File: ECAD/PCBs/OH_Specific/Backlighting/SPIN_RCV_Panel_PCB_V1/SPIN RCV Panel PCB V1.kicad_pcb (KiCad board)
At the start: 2 copper layers, 45.7 x 168.3 mm, 66 parts, among them J1 Conn_01x04_Female, J2 Conn_01x04_Female

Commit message: Latest backlighting changes
Update to multiple PCBs, mainly changing from micro-fit to mini-fit connectors.
Also changing from individual power rails to filled copper planes where possible.
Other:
- board text added: "Version 2.0"
- board text removed: "Version 1.0"

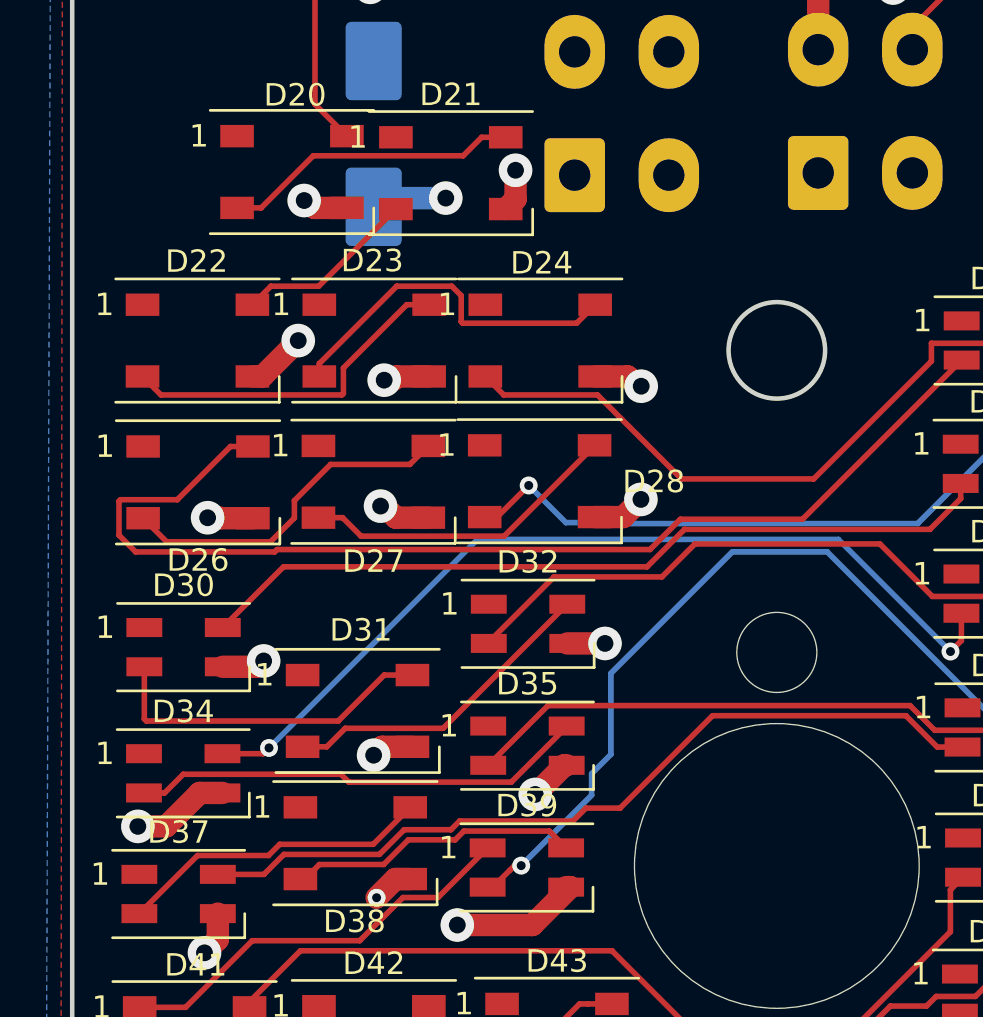
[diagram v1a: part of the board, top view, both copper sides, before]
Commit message: Backlighting PCB Updates
Added - Master mode button mounting holes to Master Arm panel
Added - ECM Jett button mounting holes to ECM JETT panel.
Added - Silkscreens to VID RCD PCB
Added - Ready LED to VID RCD PCB
Added - Manufacturing files for VID RCD PCB
Added - Manufacturing files for SPIN RCVY PCB
Added - Manufacturing files for MASTER ARM PCB
Added - Manufacturing files for ECM JETT PCB
Added - Manufacturing files for HUD PCB
Added - Manufacturing files for DEFOG LEVER PCB
Added - Manufacturing files for AV COOL PCB
Added - Manufacturing files for LDG WING FOLD PCB
Added - Extra backlighting string port to power distro PCB
Added - External power input connector to power distro PCB if ATX PSU cannot provide enough 5V current.
Added - Fan voltage selector on power distro PCB
Changed - Power distro PCB is now a solid copper fill on both sides to improve voltage drop under load.
Changed - VID RCD panel connectors to mini-fit
Changed - VID RCD panel LED pads from solid to thermal relief.
Changed - ECM JETT panel LED pads from solid to thermal relief.
Changed - MASTER ARM panel LED pads from solid to thermal relief.
Changed - SPIN RCVY panel LED pads from solid to thermal relief.
Changed - INTR LT panel LED pads from solid to thermal relief.
Changed - AV COOL panel LED pads from solid to thermal relief.
Changed - LDG WING FOLD panel LED pads from solid to thermal relief.
Changed - HUD panel LED pads from solid to thermal relief.
Changed - HUD panel connectors to mini-fit
Changed - JETT STATION SELECT PLACARD PCB connector to mini-fit
Fixed - Fan headers on power distro PCB mis-wired.
Removed - 1 row of LEDs on DEFOG PCB to improve reparability.
Removed - Version 1 folder from repo when it is replaced with a version 2 folder.
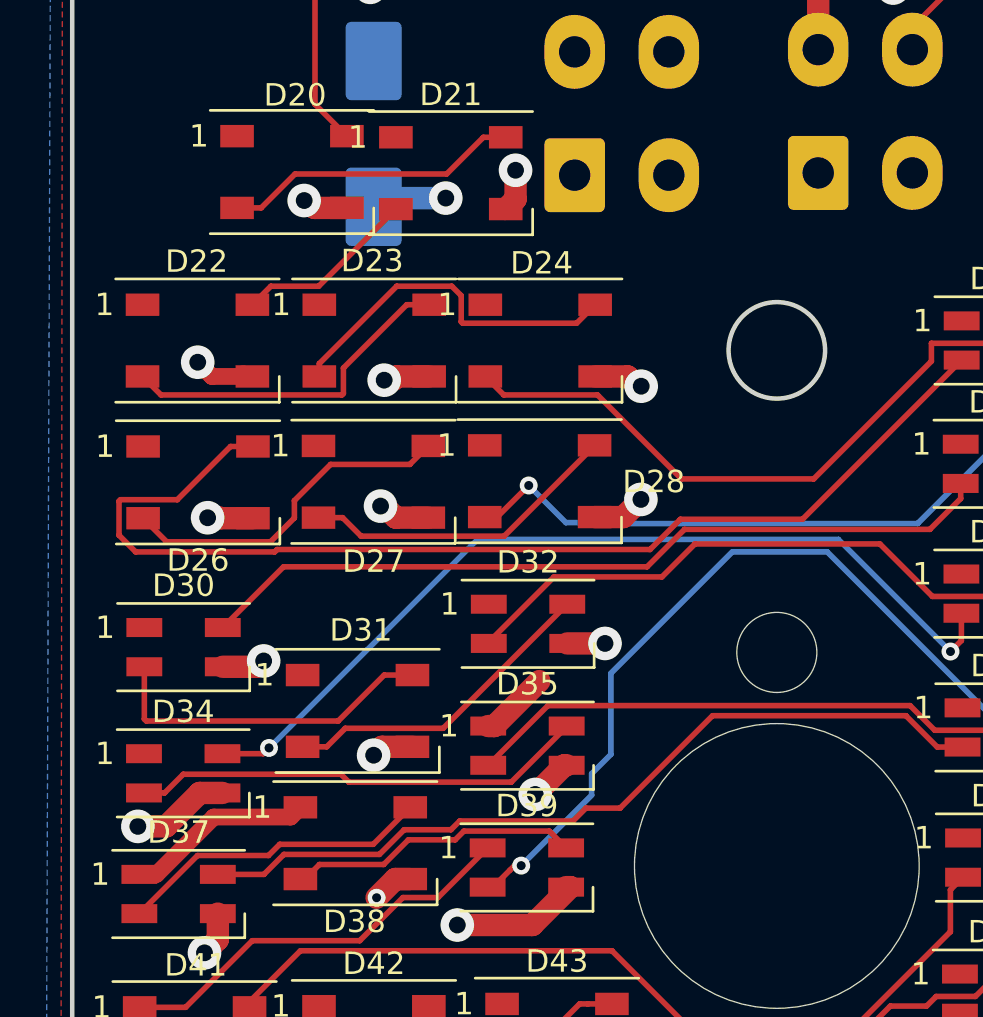
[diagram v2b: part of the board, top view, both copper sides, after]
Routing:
- net /LED+5V: track 54.2 -> 65.8 mm

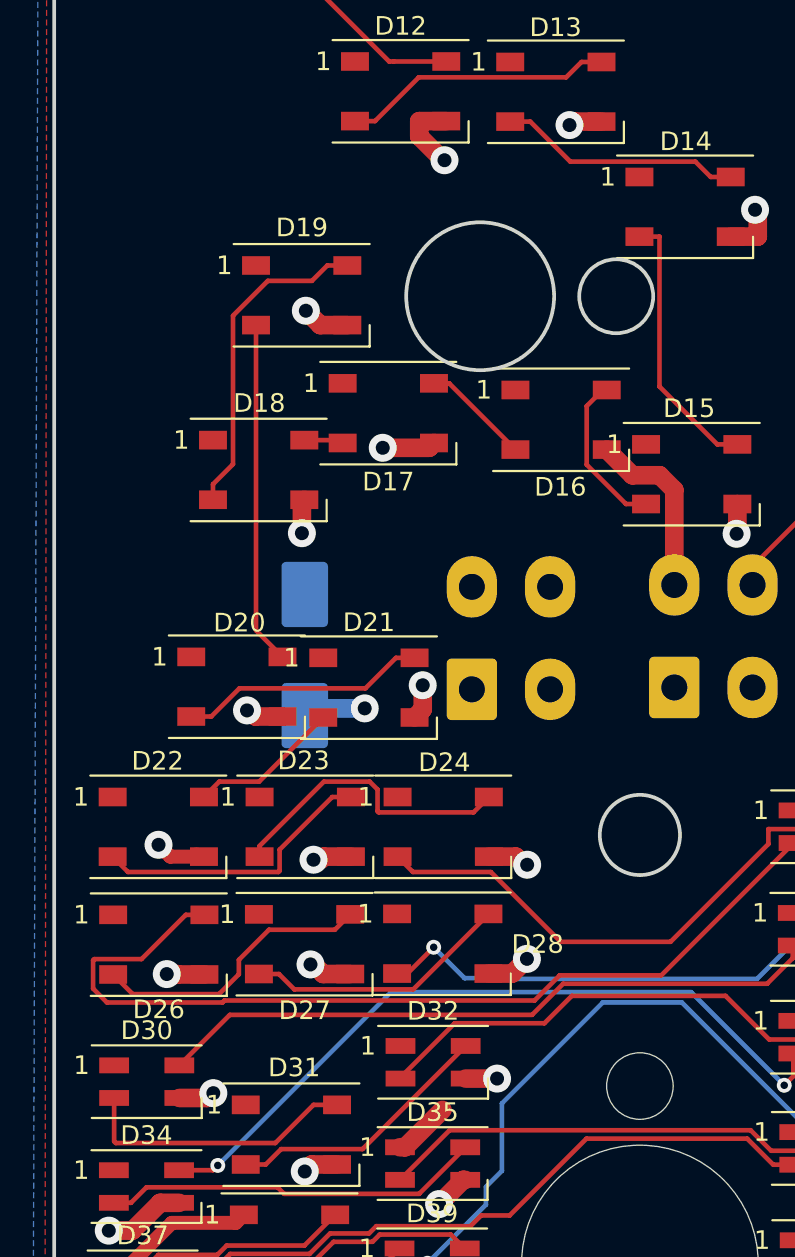
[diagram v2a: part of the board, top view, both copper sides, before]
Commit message: GEN TIE Panel overhaul and backlighting added.
Added - Gen Tie panel lightplate
Added - Gen Tie panel legend plate
Added - Gen Tie panel backlighting PCB
Added - Gen Tie panel backlighting PCB MCAD model to Gen Tie panel MCAD assembly.
Moved - ABSIS backlighting controller manufacturing files to a folder called manufacturing
Added - Fabrication notes to ABSIS backlighting controller PCB.
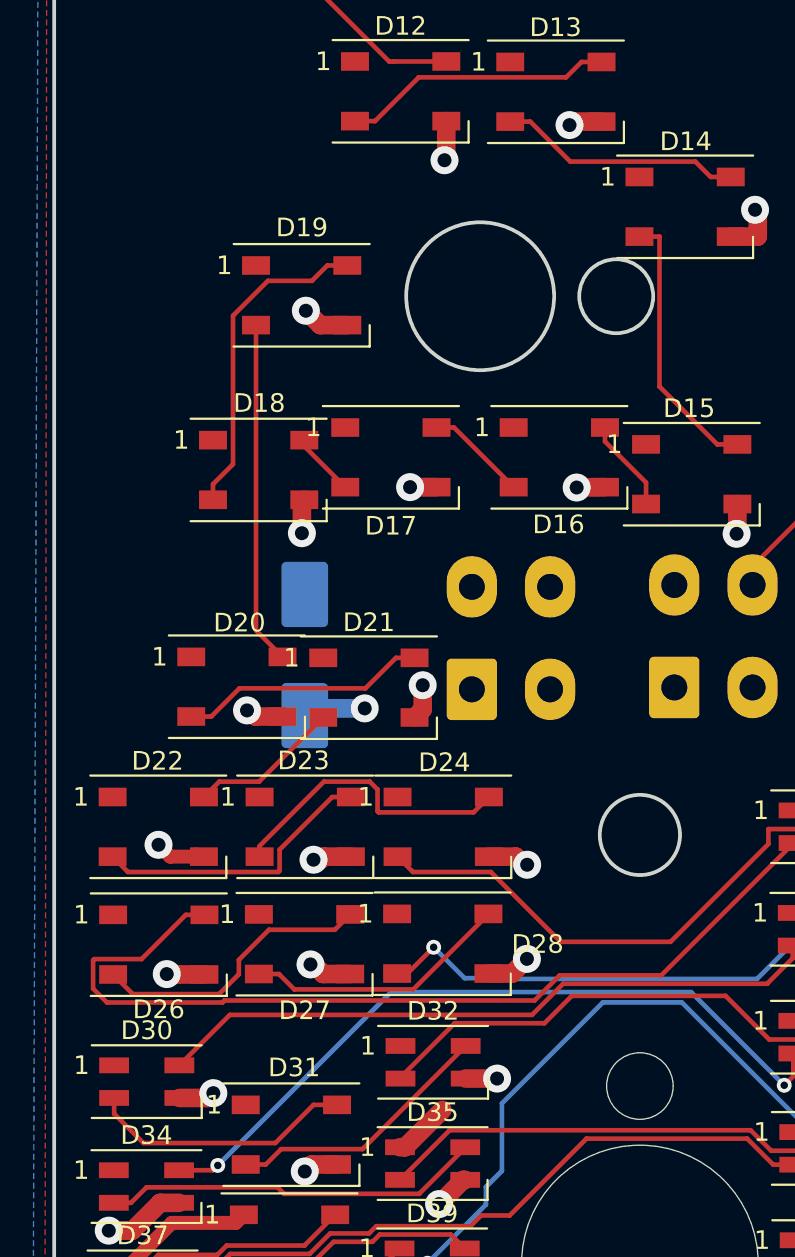
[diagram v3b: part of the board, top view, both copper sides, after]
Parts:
- moved D17 2.37 mm to (248.7, 90.0)
- moved D16 2.02 mm to (257.7, 90.0)
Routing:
- net /LEDGND: track 131.6 -> 120.0 mm, vias 52 -> 53
- net Net-(D15-Pad2): track 8.64 -> 5.02 mm
- net Net-(D17-Pad2): track 2.12 -> 3.43 mm
- net Net-(D30-Pad2): track 15.2 -> 14.3 mm
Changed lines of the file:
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@@
-(kicad_pcb (version 20171130) (host pcbnew "(5.1.6)-1")
+(kicad_pcb (version 20171130) (host pcbnew "(5.1.10)-1")
   (general
     (thickness 1.6)
-    (drawings 236)
-    (tracks 546)
+    (drawings 237)
+    (tracks 541)
     (zones 0)
     (modules 66)
@@
   )
   (module LED_SMD:LED_WS2812B_PLCC4_5.0x5.0mm_P3.2mm (layer F.Cu)
-    (at 248.553 87.579)
+    (at 248.69 89.95)
     (descr https://cdn-shop.adafruit.com/datasheets/WS2812B.pdf)
     (tags "LED RGB NeoPixel")
@@
   )
   (module LED_SMD:LED_WS2812B_PLCC4_5.0x5.0mm_P3.2mm (layer F.Cu)
-    (at 257.824 87.9346)
+    (at 257.73 89.95)
     (descr https://cdn-shop.adafruit.com/datasheets/WS2812B.pdf)
     (tags "LED RGB NeoPixel")
@@
     )
   )
+  (gr_circle (center 253.481123 81.304936) (end 259.981123 81.304936) (layer Dwgs.User) (width 0.15))
   (gr_line (start 252.76829 27.873681) (end 252.76829 33.073681) (layer Dwgs.User) (width 0.2))
   (gr_text "SPIN RCVRY" (at 250.444 133.2484) (layer B.SilkS)
@@
     (effects (font (size 1 1) (thickness 0.15)) (justify left mirror))
   )
-  (segment (start 251.663 71.907) (end 250.2127 71.907) (width 1) (layer F.Cu) (net 1))
-  (segment (start 251.5679 74.006) (end 251.4936 74.006) (width 1) (layer F.Cu) (net 1))
-  (segment (start 251.4936 74.006) (end 250.2127 72.7251) (width 1) (layer F.Cu) (net 1))
-  (segment (start 250.2127 72.7251) (end 250.2127 71.907) (width 1) (layer F.Cu) (net 1))
   (segment (start 267.2442 94.0528) (end 267.284 94.013) (width 1) (layer F.Cu) (net 1))
   (segment (start 267.284 94.013) (end 267.284 92.4556) (width 1) (layer F.Cu) (net 1))
@@
   (segment (start 236.6617 117.6818) (end 237.2125 117.6818) (width 1) (layer F.Cu) (net 1))
   (segment (start 237.2125 117.6818) (end 237.2337 117.703) (width 1) (layer F.Cu) (net 1))
-  (segment (start 263.9 96.8) (end 263.9 91.6988) (width 1) (layer F.Cu) (net 1))
-  (segment (start 263.9 91.6988) (end 263.1144 90.9132) (width 1) (layer F.Cu) (net 1))
-  (segment (start 263.1144 90.9132) (end 261.6526 90.9132) (width 1) (layer F.Cu) (net 1))
-  (segment (start 261.6526 90.9132) (end 260.274 89.5346) (width 1) (layer F.Cu) (net 1))
   (segment (start 273.558 157.35) (end 275.0583 157.35) (width 1) (layer F.Cu) (net 1))
   (segment (start 275.3445 157.4649) (end 275.1732 157.4649) (width 1) (layer F.Cu) (net 1))
@@
   (via (at 275.3445 157.4649) (size 1.5) (drill 0.75) (layers F.Cu B.Cu) (net 1))
   (via (at 259.9618 32.1029) (size 1.5) (drill 0.75) (layers F.Cu B.Cu) (net 1))
-  (via (at 248.2538 89.4381) (size 1.5) (drill 0.75) (layers F.Cu B.Cu) (net 1))
   (via (at 250.3985 102.1812) (size 1.5) (drill 0.75) (layers F.Cu B.Cu) (net 1))
   (via (at 244.1272 82.0828) (size 1.5) (drill 0.75) (layers F.Cu B.Cu) (net 1))
@@
   (segment (start 243.9145 92.3555) (end 244.043 92.227) (width 1) (layer F.Cu) (net 1))
   (segment (start 243.9145 94.0211) (end 243.9145 92.3555) (width 1) (layer F.Cu) (net 1))
-  (segment (start 250.7439 89.4381) (end 251.003 89.179) (width 1) (layer F.Cu) (net 1))
-  (segment (start 248.2538 89.4381) (end 250.7439 89.4381) (width 1) (layer F.Cu) (net 1))
   (segment (start 247.394 59.334) (end 247.4 61.15) (width 1) (layer F.Cu) (net 1))
   (segment (start 247.4 61.15) (end 247.394 61.144) (width 1) (layer F.Cu) (net 1))
@@
   (segment (start 236.22 110.744) (end 236.22 110.744) (width 0.75) (layer F.Cu) (net 1))
   (via (at 236.22 110.744) (size 1.5) (drill 0.75) (layers F.Cu B.Cu) (net 1))
+  (segment (start 251.663 73.9109) (end 251.5679 74.006) (width 1) (layer F.Cu) (net 1))
+  (segment (start 251.663 71.907) (end 251.663 73.9109) (width 1) (layer F.Cu) (net 1))
+  (segment (start 251.14 91.55) (end 249.72 91.55) (width 1) (layer F.Cu) (net 1))
+  (segment (start 249.72 91.55) (end 249.72 91.55) (width 1) (layer F.Cu) (net 1))
+  (via (at 249.72 91.55) (size 1.5) (drill 0.75) (layers F.Cu B.Cu) (net 1))
+  (segment (start 260.18 91.55) (end 258.66 91.57) (width 1) (layer F.Cu) (net 1))
+  (segment (start 258.66 91.57) (end 258.68 91.55) (width 1) (layer F.Cu) (net 1))
+  (via (at 258.66 91.57) (size 1.5) (drill 0.75) (layers F.Cu B.Cu) (net 1))
   (segment (start 247.286 103.4228) (end 244.4552 103.4228) (width 1) (layer B.Cu) (net 2))
   (segment (start 244.4552 103.4228) (end 244.069 103.809) (width 1) (layer B.Cu) (net 2))
@@
   (segment (start 263.1043 78.1046) (end 263.1043 86.1512) (width 0.25) (layer F.Cu) (net 16))
   (segment (start 263.1043 86.1512) (end 266.2087 89.2556) (width 0.25) (layer F.Cu) (net 16))
-  (segment (start 262.384 92.4556) (end 261.3087 92.4556) (width 0.25) (layer F.Cu) (net 17))
-  (segment (start 261.3087 92.4556) (end 259.1987 90.3456) (width 0.25) (layer F.Cu) (net 17))
-  (segment (start 260.0628 86.3346) (end 259.1987 87.1987) (width 0.25) (layer F.Cu) (net 17))
-  (segment (start 260.274 86.3346) (end 260.0628 86.3346) (width 0.25) (layer F.Cu) (net 17))
-  (segment (start 259.1987 90.3456) (end 259.1987 87.1987) (width 0.25) (layer F.Cu) (net 17))
-  (segment (start 251.8184 85.979) (end 255.374 89.5346) (width 0.25) (layer F.Cu) (net 18))
-  (segment (start 251.003 85.979) (end 251.8184 85.979) (width 0.25) (layer F.Cu) (net 18))
-  (segment (start 245.951 89.027) (end 246.103 89.179) (width 0.25) (layer F.Cu) (net 19))
-  (segment (start 244.043 89.027) (end 245.951 89.027) (width 0.25) (layer F.Cu) (net 19))
+  (segment (start 262.384 91.304) (end 262.384 92.4556) (width 0.25) (layer F.Cu) (net 17))
+  (segment (start 260.18 89.1) (end 262.384 91.304) (width 0.25) (layer F.Cu) (net 17))
+  (segment (start 260.18 88.35) (end 260.18 89.1) (width 0.25) (layer F.Cu) (net 17))
+  (segment (start 252.08 88.35) (end 255.28 91.55) (width 0.25) (layer F.Cu) (net 18))
+  (segment (start 251.14 88.35) (end 252.08 88.35) (width 0.25) (layer F.Cu) (net 18))
+  (segment (start 244.043 89.353) (end 246.24 91.55) (width 0.25) (layer F.Cu) (net 19))
+  (segment (start 244.043 89.027) (end 244.043 89.353) (width 0.25) (layer F.Cu) (net 19))
   (segment (start 246.352 79.6544) (end 245.2767 79.6544) (width 0.25) (layer F.Cu) (net 20))
   (segment (start 240.2183 82.348) (end 242.0866 80.4797) (width 0.25) (layer F.Cu) (net 20))
@@
   (segment (start 257.9364 118.20001) (end 256.26521 119.8712) (width 0.25) (layer F.Cu) (net 30))
   (segment (start 256.26521 119.8712) (end 240.0468 119.8712) (width 0.25) (layer F.Cu) (net 30))
-  (segment (start 233.838 124.33) (end 233.838 126.662) (width 0.25) (layer F.Cu) (net 31))
-  (segment (start 233.838 126.662) (end 233.926 126.75) (width 0.25) (layer F.Cu) (net 31))
   (segment (start 244.53889 124.7) (end 245.8 124.7) (width 0.25) (layer F.Cu) (net 31))
   (segment (start 242.48889 126.75) (end 244.53889 124.7) (width 0.25) (layer F.Cu) (net 31))
-  (segment (start 233.926 126.75) (end 242.48889 126.75) (width 0.25) (layer F.Cu) (net 31))
+  (segment (start 233.838 125.178) (end 235.41 126.75) (width 0.25) (layer F.Cu) (net 31))
+  (segment (start 233.838 124.33) (end 233.838 125.178) (width 0.25) (layer F.Cu) (net 31))
+  (segment (start 235.41 126.75) (end 242.48889 126.75) (width 0.25) (layer F.Cu) (net 31))
   (segment (start 240.9 127.9) (end 241.9753 127.9) (width 0.25) (layer F.Cu) (net 32))
   (segment (start 241.9753 127.9) (end 242.8006 127.0747) (width 0.25) (layer F.Cu) (net 32))
